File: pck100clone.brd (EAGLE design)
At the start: 72.4 x 68.6 mm, 92 parts, among them IC1 LM358N, IC3 LM358N, IC4 LM358N, IC5 LM358N, Q1 2SC945, Q2 2SC945, Q3 2N3906, Q4 2N3906, Q5 2N3904, Q6 2N3904

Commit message: tweaks
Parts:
- renumbered R100 to R44
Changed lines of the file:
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@@
 <attribute name="VALUE" x="11.049" y="32.385" size="1.27" layer="27" ratio="10" rot="R270"/>
 </element>
-<element name="R100" library="rcl" package="0207/7" value="4k7" x="17.78" y="40.005" smashed="yes" rot="R180">
+<element name="R44" library="rcl" package="0207/7" value="4k7" x="17.78" y="40.005" smashed="yes" rot="R180">
 <attribute name="NAME" x="19.685" y="40.513" size="1.27" layer="25" ratio="10" rot="R180"/>
 </element>
@@
 <contactref element="OUT" pad="3"/>
 <contactref element="IC4" pad="4"/>
-<contactref element="R100" pad="1"/>
+<contactref element="R44" pad="1"/>
 <contactref element="Q5" pad="3"/>
 <contactref element="Q6" pad="3"/>
@@
 </signal>
 <signal name="N$44">
-<contactref element="R100" pad="2"/>
+<contactref element="R44" pad="2"/>
 <contactref element="PWR" pad="K"/>
 <wire x1="12.7" y1="33.02" x2="15.24" y2="35.56" width="0.4064" layer="1"/>

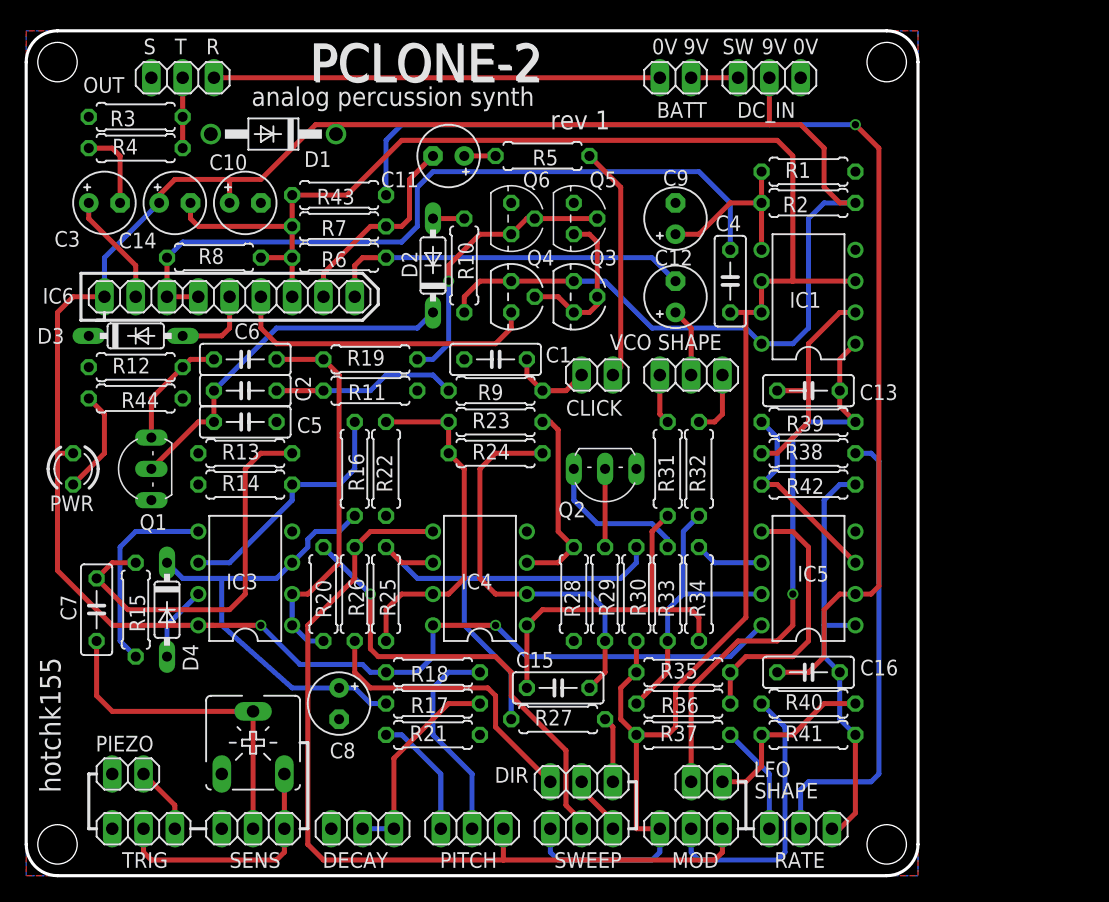
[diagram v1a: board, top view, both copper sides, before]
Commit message: added VCA pulldown
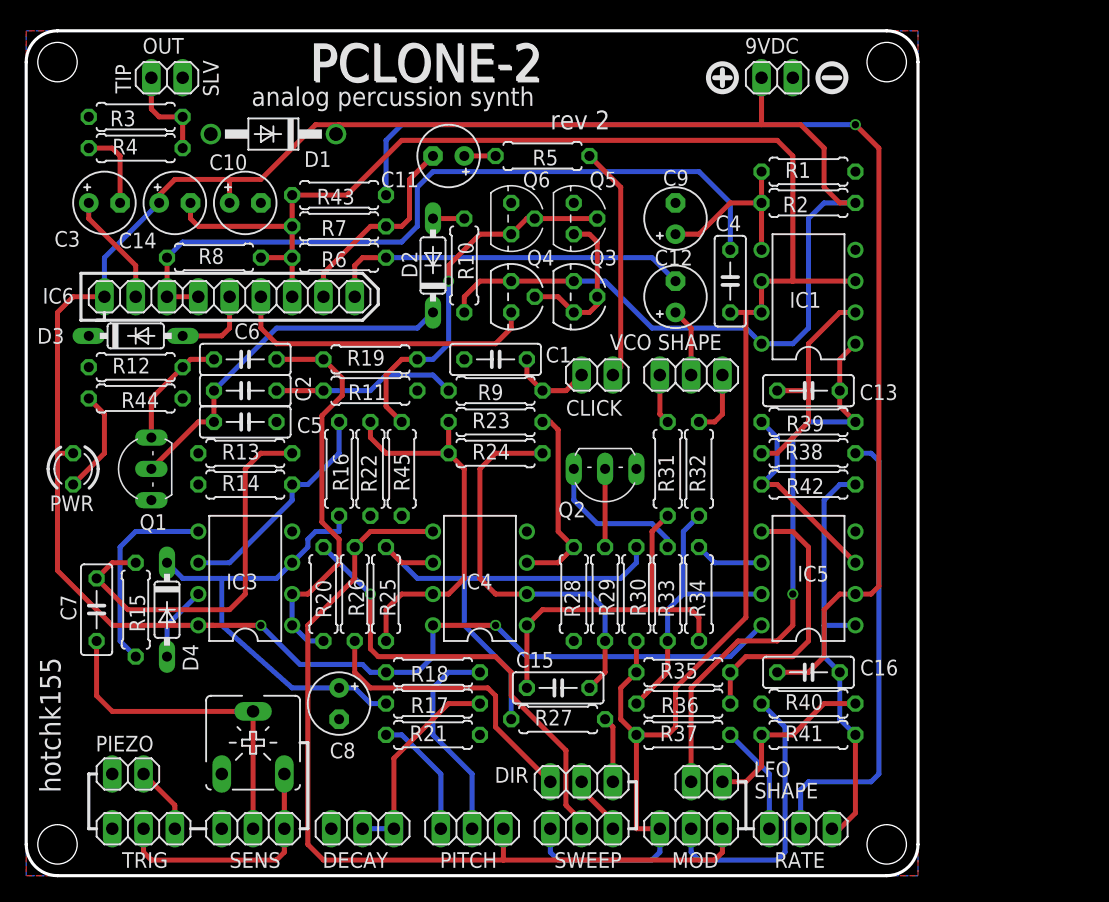
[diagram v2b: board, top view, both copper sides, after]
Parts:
- removed BATT: (no value), pinhead:1X02
- removed DC_IN: (no value), pinhead:1X03
- added 9VDC: (no value), pinhead:1X02
- added R45: 10k, rcl:0207/7
- OUT: device pinhead:1X03 -> pinhead:1X02
- moved R16 1.27 mm to (34.3, 34.3)
- moved R22 1.27 mm to (36.8, 34.3)
- moved OUT 1.27 mm to (20.3, 66.0), turned to 0 degrees
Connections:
- removed net N$50: BATT.2, OUT.1
- removed net N$54: BATT.1, DC_IN.1
- net BA662_1: now also R45.1
- net GND: now also 9VDC.2, OUT.2, R45.2; no longer DC_IN.3, OUT.3
- net OUT: now also OUT.1; no longer OUT.2
- net VCC: now also 9VDC.1; no longer DC_IN.2
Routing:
- net N$50: track 36.2 -> 0.00 mm
- net BA662_1: track 23.1 -> 30.5 mm
- net N$54: track 3.81 -> 0.00 mm
- net N$32: track 28.2 -> 31.3 mm
- net OUT: track 5.72 -> 7.88 mm
- net N$6: track 20.4 -> 18.4 mm
- net TRIGGER: track 31.3 -> 32.7 mm
- net N$8: track 37.8 -> 37.3 mm
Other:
- board text added: "SLV"
- board text added: "TIP"
- board text added: "rev 2"
- board text removed: "0V"
- board text removed: "9V"
- board text removed: "R"
- board text removed: "S"
- board text removed: "SW"
- board text removed: "T"
- board text removed: "rev 1"

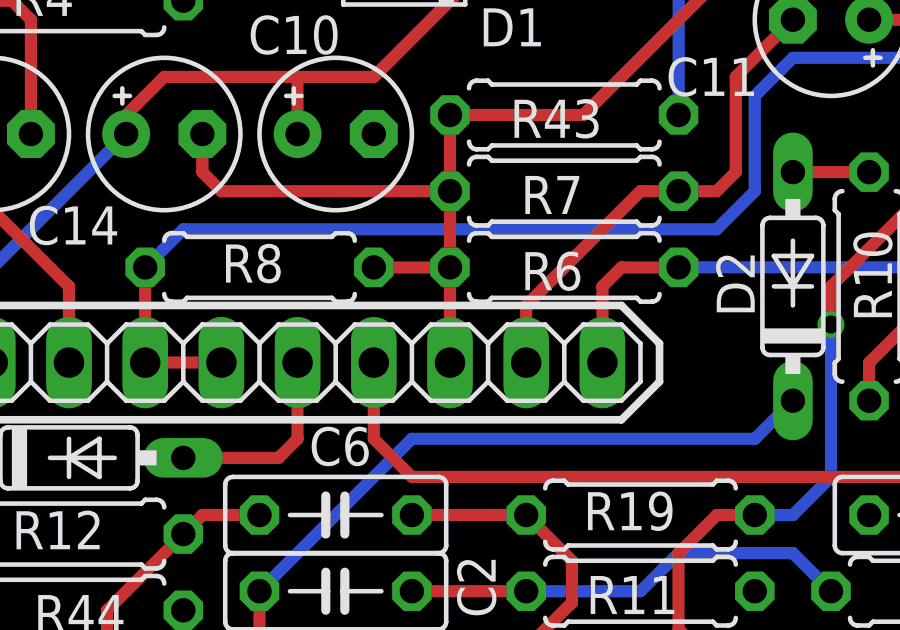
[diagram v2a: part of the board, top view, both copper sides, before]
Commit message: remove VCA pin 3 connection to VGND
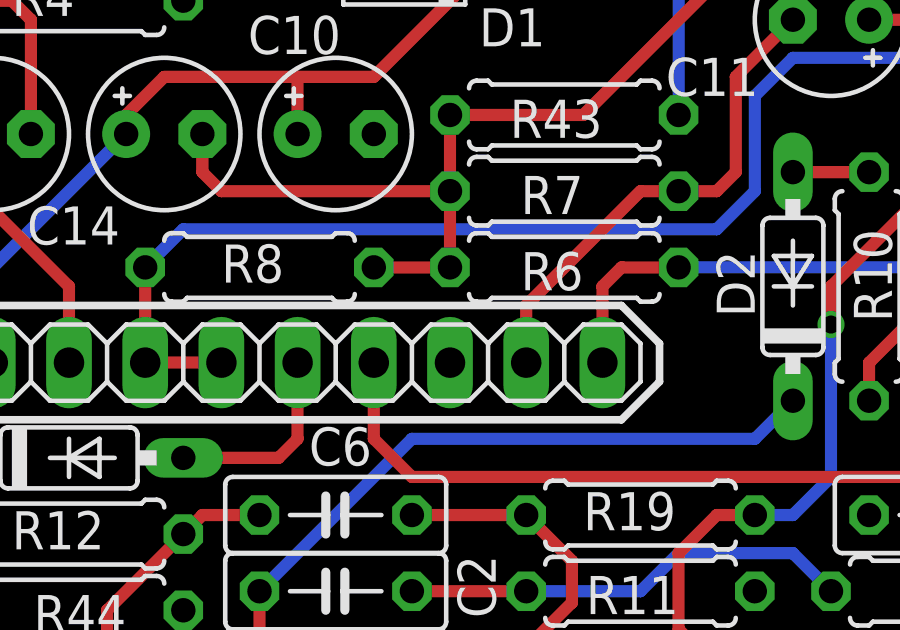
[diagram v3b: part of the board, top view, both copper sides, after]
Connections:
- net VGND: no longer IC6.3
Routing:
- net VGND: track 157.3 -> 154.2 mm
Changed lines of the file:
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@@
 <contactref element="C4" pad="1"/>
 <contactref element="SWEEP" pad="3"/>
-<contactref element="IC6" pad="3"/>
 <wire x1="58.42" y1="20.32" x2="58.42" y2="17.78" width="0.4064" layer="1"/>
 <wire x1="58.42" y1="12.7" x2="57.15" y2="13.97" width="0.4064" layer="1"/>
@@
 <wire x1="66.04" y1="46.99" x2="67.31" y2="46.99" width="0.4064" layer="1"/>
 <wire x1="67.31" y1="46.99" x2="68.58" y2="46.99" width="0.4064" layer="1"/>
-<wire x1="30.48" y1="51.435" x2="30.48" y2="48.26" width="0.4064" layer="1"/>
 <wire x1="27.94" y1="51.435" x2="30.48" y2="51.435" width="0.4064" layer="1"/>
 <wire x1="22.225" y1="55.88" x2="22.225" y2="54.61" width="0.4064" layer="1"/>

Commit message: moar stuff
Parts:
- removed ATTACK, PIEZO, SHAPE: (no value), pinhead:1X02
- removed DIR, TRIG: (no value), pinhead:1X03
- removed SENS_LEVEL: (no value), pot:CA6V
- added CLICK: (no value), pinhead:1X03
- added INPUT, SHP: (no value), pinhead:1X02
- SWEEP: device pinhead:1X03 -> pinhead:1X04
- moved MOD 5.68 mm to (57.8, 7.62)
- moved PITCH 5.68 mm to (40.0, 7.62)
- moved SWEEP 5.68 mm to (48.9, 7.62), turned to 0 degrees
- moved DECAY 4.58 mm to (32.4, 7.62)
- moved SENS 3.59 mm to (24.8, 7.62)
- moved RATE 2.84 mm to (70.5, 7.62)
- moved WAVE 1.27 mm to (62.9, 43.2)
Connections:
- removed net N$18: DIR.2, SWEEP.1
- removed net N$2: SENS.1, SENS_LEVEL.E, TRIG.2
- net ATTACK_OUT: now also CLICK.2; no longer ATTACK.2
- net GND: now also INPUT.1; no longer PIEZO.1, SENS_LEVEL.A, TRIG.3
- net MOD_OUT: now also SHP.2; no longer SHAPE.2
- net N$1: now also INPUT.2, SENS.1; no longer PIEZO.2, TRIG.1
- net N$14: now also CLICK.1; no longer ATTACK.1
- net N$15: now also SHP.1; no longer SHAPE.1
- net N$21: now also SWEEP.3; no longer SWEEP.2
- net N$24: now also SWEEP.4; no longer DIR.3
- net N$25: now also SWEEP.2; no longer DIR.1
- net N$3: no longer SENS_LEVEL.S
- net VGND: now also SWEEP.1; no longer SWEEP.3
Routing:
- net N$2: track 20.2 -> 0.00 mm
- net N$28: track 22.9 -> 15.1 mm
- net N$1: track 5.50 -> 12.0 mm
- net N$3: track 27.2 -> 21.0 mm
- net N$27: track 71.5 -> 65.7 mm
- net N$14: track 6.77 -> 12.0 mm
- net N$30: track 10.2 -> 5.34 mm
- net N$18: track 4.86 -> 0.00 mm
- net N$21: track 37.1 -> 33.0 mm
- net N$22: track 8.94 -> 5.87 mm
- net N$29: track 17.1 -> 14.0 mm
- net N$24: track 5.34 -> 8.41 mm
- net N$9: track 17.1 -> 19.1 mm
- net VGND: track 154.2 -> 152.3 mm
- net N$17: track 37.6 -> 36.3 mm
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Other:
- board text added: "WAVE"
- board text removed: "CLICK"
- board text removed: "VCO SHAPE"

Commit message: cv patch point
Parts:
- added JP1: (no value), pinhead:1X01
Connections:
- net N$8: now also JP1.1
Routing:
- net N$8: track 37.3 -> 38.1 mm
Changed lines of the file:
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@@
 <attribute name="VALUE" x="59.055" y="46.355" size="1.27" layer="27" rot="R180"/>
+</element>
+<element name="JP1" library="pinhead" package="1X01" value="" x="26.67" y="18.669" smashed="yes">
+<attribute name="VALUE" x="25.4" y="15.494" size="1.27" layer="27"/>
 </element>
 </elements>
@@
 <wire x1="31.75" y1="28.575" x2="31.75" y2="27.94" width="0.4064" layer="16"/>
 <wire x1="31.75" y1="27.94" x2="30.48" y2="26.67" width="0.4064" layer="16"/>
-<wire x1="34.29" y1="16.51" x2="30.48" y2="16.51" width="0.4064" layer="16"/>
-<wire x1="30.48" y1="16.51" x2="24.765" y2="21.59" width="0.4064" layer="16"/>
+<wire x1="34.29" y1="16.51" x2="28.829" y2="16.51" width="0.4064" layer="16"/>
 <wire x1="34.29" y1="16.51" x2="35.56" y2="16.51" width="0.4064" layer="16"/>
 <wire x1="35.56" y1="16.51" x2="36.83" y2="15.24" width="0.4064" layer="16"/>
 <wire x1="36.83" y1="15.24" x2="38.1" y2="15.24" width="0.4064" layer="16"/>
-<wire x1="24.765" y1="21.59" x2="24.765" y2="25.4" width="0.4064" layer="16"/>
+<wire x1="24.765" y1="20.574" x2="24.765" y2="25.4" width="0.4064" layer="16"/>
+<contactref element="JP1" pad="1"/>
+<wire x1="24.765" y1="20.574" x2="26.67" y2="18.669" width="0.4064" layer="16"/>
+<wire x1="28.829" y1="16.51" x2="26.67" y2="18.669" width="0.4064" layer="16"/>
 </signal>
 <signal name="N$9">

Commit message: work in progress
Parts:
- removed INPUT: (no value), pinhead:1X02
- removed MOD: (no value), pinhead:1X03
- added DEPTH: (no value), pinhead:1X03
- added TRIG: (no value), pinhead:1X02
- moved 9VDC 4.02 mm to (73.7, 67.3)
- moved OUT 4.02 mm to (16.5, 67.3), turned to 180 degrees
- moved DECAY 3.81 mm to (32.4, 3.81)
- moved PITCH 3.81 mm to (40.0, 3.81)
- moved RATE 3.81 mm to (70.5, 3.81)
- moved SENS 3.81 mm to (24.8, 3.81)
- moved SHP 3.81 mm to (64.1, 3.81)
- moved SWEEP 3.81 mm to (48.9, 3.81)
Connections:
- net GND: now also TRIG.1; no longer INPUT.1
- net N$1: now also TRIG.2; no longer INPUT.2
- net N$27: now also DEPTH.1; no longer MOD.1
- net N$28: now also DEPTH.2; no longer MOD.2
- net VGND: now also DEPTH.3; no longer MOD.3
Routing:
- net VGND: track 152.3 -> 156.5 mm
- net N$9: track 19.1 -> 22.9 mm
- net N$21: track 33.0 -> 36.8 mm
- net N$17: track 36.3 -> 40.2 mm
- net N$15: track 47.5 -> 51.3 mm
- net N$22: track 5.87 -> 9.68 mm
- net N$30: track 5.34 -> 9.15 mm
- net N$3: track 21.0 -> 24.8 mm
- net N$29: track 14.0 -> 17.8 mm, vias 0 -> 1
- net N$25: track 23.3 -> 27.1 mm
- net N$24: track 8.41 -> 12.2 mm
- net MOD_OUT: track 15.1 -> 18.9 mm
- net N$28: track 15.1 -> 18.1 mm, vias 0 -> 1
- net N$20: track 33.2 -> 35.9 mm
- net N$1: track 12.0 -> 14.5 mm
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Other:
- board text added: "/pclone2"
- board text added: "six4pix.com"
- board text removed: "SLV"
